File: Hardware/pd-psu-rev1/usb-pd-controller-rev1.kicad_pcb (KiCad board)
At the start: 2 copper layers, 22 parts, among them CN3 KF301-2P, J2 USB_C_Receptacle_USB2.0_16P, SW1 RotaryEncoder_Switch, U1 INA219AxD, U2 CH224K, U3 CH32V003FxPx, U4 78L33

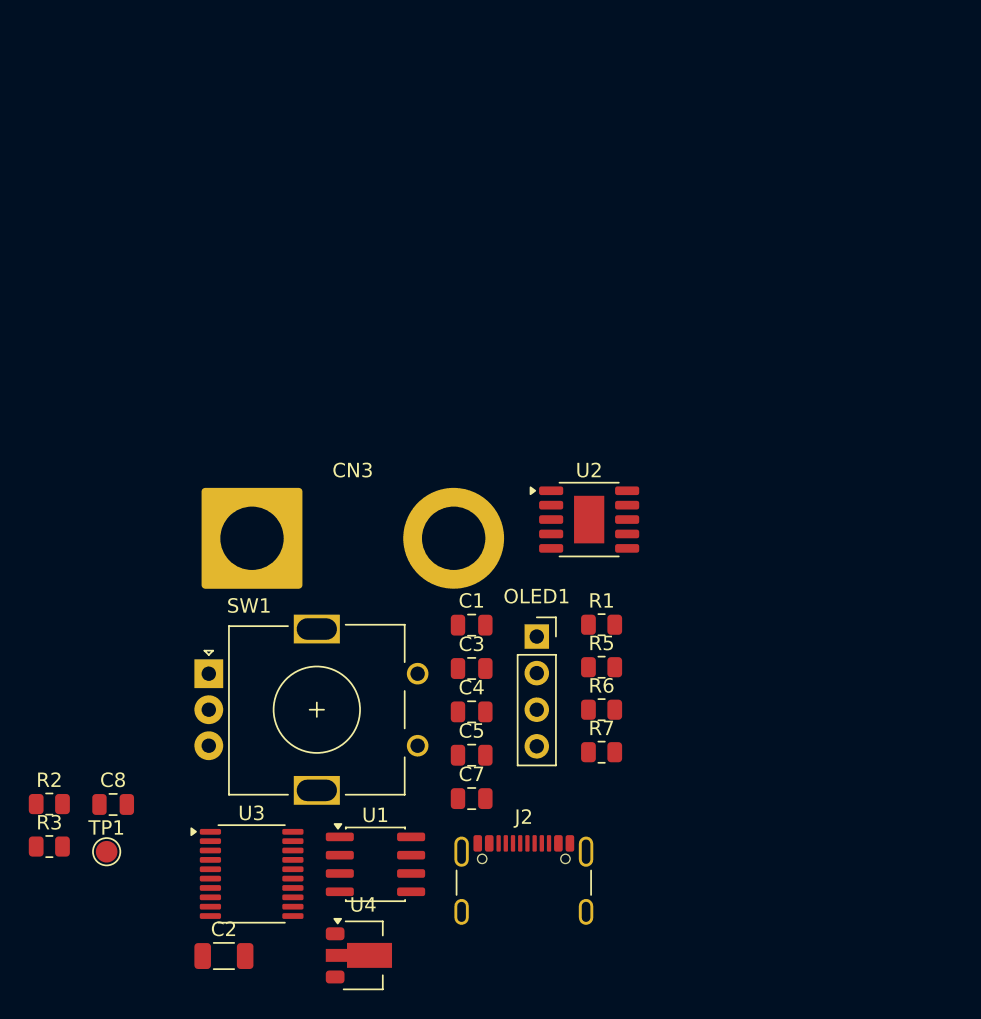
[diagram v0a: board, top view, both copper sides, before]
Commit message: update schematic
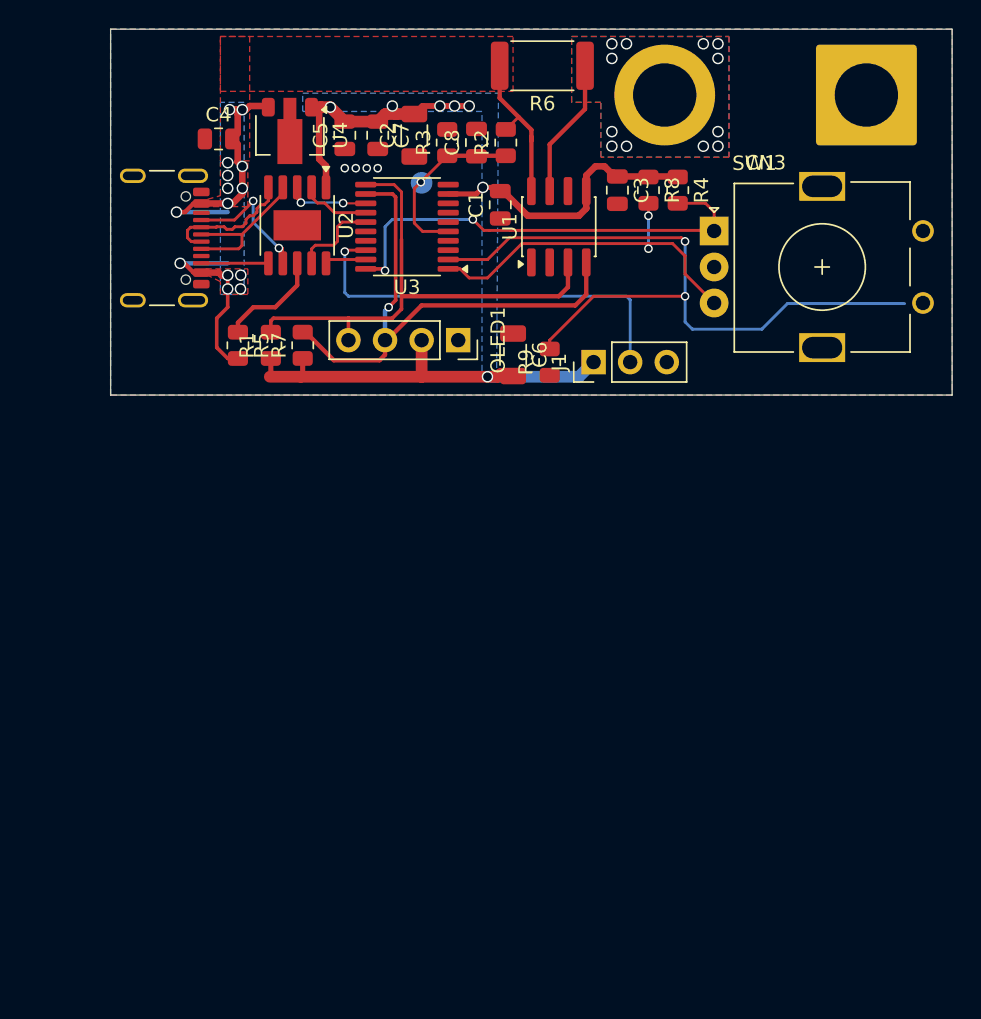
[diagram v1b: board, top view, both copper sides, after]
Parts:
- added C6: 10u, Capacitor_SMD:C_1206_3216Metric, F.Cu at (152.4, 65.8)
- added J1: Conn_01x03, Connector_PinHeader_2.54mm:PinHeader_1x03_P2.54mm_Vertical, F.Cu at (158.0, 66.3)
- added R4: 10K, Resistor_SMD:R_0805_2012Metric, F.Cu at (163.8, 54.4)
- added R8: 10K, Resistor_SMD:R_0805_2012Metric, F.Cu at (161.8, 54.4)
- added R9: 10K, Resistor_SMD:R_0805_2012Metric, F.Cu at (154.9, 66.3)
- R6: footprint Resistor_SMD:R_0805_2012Metric -> Resistor_SMD:R_2512_6332Metric
- TP1: moved to B.Cu
- moved C2 58.5 mm to (145.5, 50.5), turned to 90 degrees
- moved U4 57.2 mm to (136.9, 50.5), turned to -90 degrees
- moved R3 56.1 mm to (147.8, 51.1), turned to 90 degrees
- moved R2 55.8 mm to (151.9, 51.1), turned to 90 degrees
- moved J2 52.6 mm to (127.1, 57.7), turned to -90 degrees
- moved CN3 52.6 mm to (176.9, 47.8), turned to 180 degrees
- moved C8 52.4 mm to (149.9, 51.1), turned to 90 degrees
- moved TP1 51.3 mm to (146.1, 53.8), turned to 180 degrees
- moved SW1 46.6 mm to (166.4, 57.2)
- moved C7 46.5 mm to (143.0, 50.5), turned to -90 degrees
- moved U3 46.2 mm to (145.0, 56.9), turned to 180 degrees
- moved U1 46.1 mm to (155.6, 56.9), turned to 90 degrees
- moved R6 44.9 mm to (154.4, 45.7), turned to 180 degrees
- moved C5 43.9 mm to (140.7, 50.5), turned to 90 degrees
- moved C4 43.5 mm to (132.0, 50.8)
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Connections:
- U3 pad 1: CFG2 -> ROT_B
- U3 pad 11: unconnected-(U3-PC1-Pad11) -> SDA
- U3 pad 12: ROT_A -> SCL
- U3 pad 13: unconnected-(U3-PC3-Pad13) -> CFG3
- U3 pad 14: ROT_PUSH -> CFG2
- U3 pad 15: ROT_B -> CFG1
- U3 pad 16: SDA -> unconnected-(U3-PC6-Pad16)
- U3 pad 18: SCL -> Net-(J1-Pin_2)
- U3 pad 2: CFG3 -> ROT_PUSH
- U3 pad 20: CFG1 -> ROT_A
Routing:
- net +3.3V: track 0.00 -> 68.0 mm, vias 0 -> 7
- net ROT_PUSH: track 0.00 -> 50.2 mm, vias 0 -> 2
- net VBUS: track 0.00 -> 44.1 mm, vias 0 -> 14
- net SCL: track 0.00 -> 38.0 mm, vias 0 -> 1
- net SDA: track 0.00 -> 36.3 mm
- net ROT_A: track 0.00 -> 31.8 mm, vias 0 -> 2
- net Net-(J1-Pin_2): track 0.00 -> 28.7 mm, vias 0 -> 1
- net ROT_B: track 0.00 -> 25.7 mm, vias 0 -> 2
- net Net-(U3-PA1): track 0.00 -> 12.3 mm, vias 0 -> 1
- net DP: track 0.00 -> 11.0 mm
- net VOUT: track 0.00 -> 9.72 mm, vias 0 -> 12
- net CC1: track 0.00 -> 9.47 mm, vias 0 -> 2
- net DM: track 0.00 -> 9.43 mm
- net Net-(U2-VBUS): track 0.00 -> 7.38 mm
- net CFG1: track 0.00 -> 6.13 mm
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- added copper zone on B.Cu, net +3.3V
- added copper zone on B.Cu, net GND
- added copper zone on F.Cu, net GND
- added copper zone on B.Cu, net VBUS
- added copper zone on F.Cu, net VBUS
- added copper zone on B.Cu, net VOUT
- added copper zone on F.Cu, net VOUT
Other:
- board outline added: 58.4 x 25.4 mm
